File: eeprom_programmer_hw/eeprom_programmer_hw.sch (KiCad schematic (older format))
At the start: 8 parts

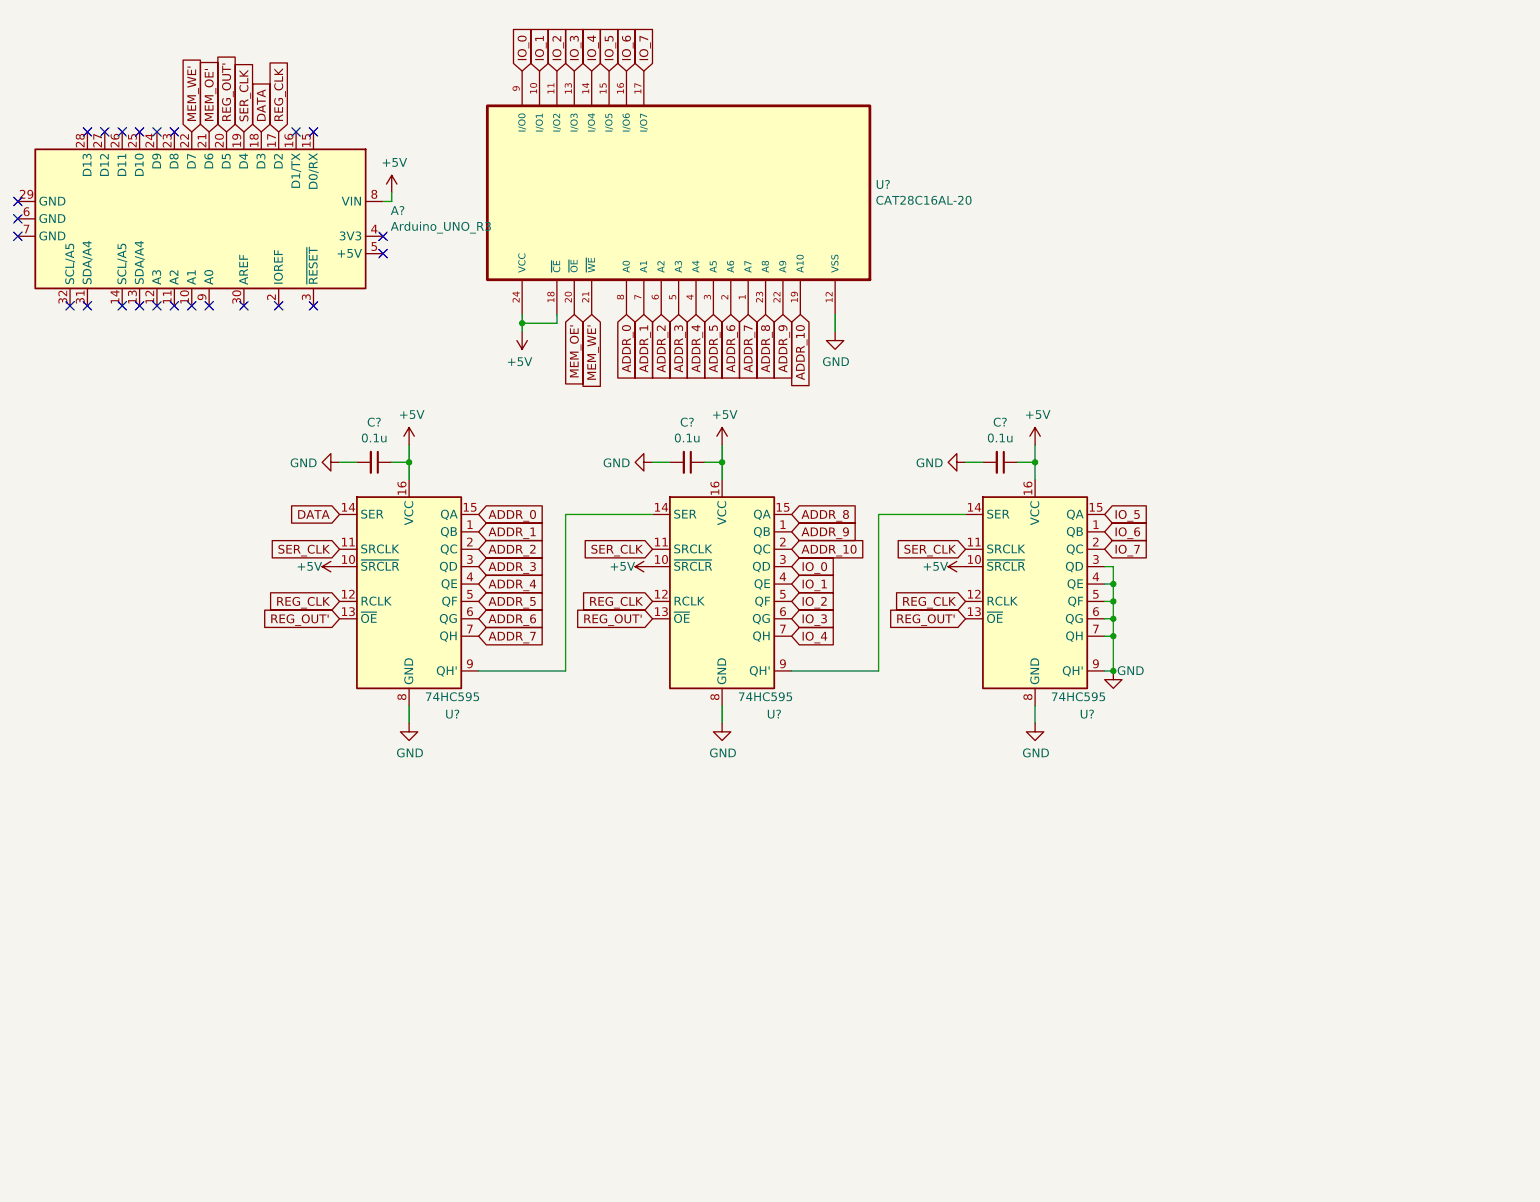
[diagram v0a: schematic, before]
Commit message: Added tri-state buffers to regulate output of shift registers when interating with eeprom I/O.
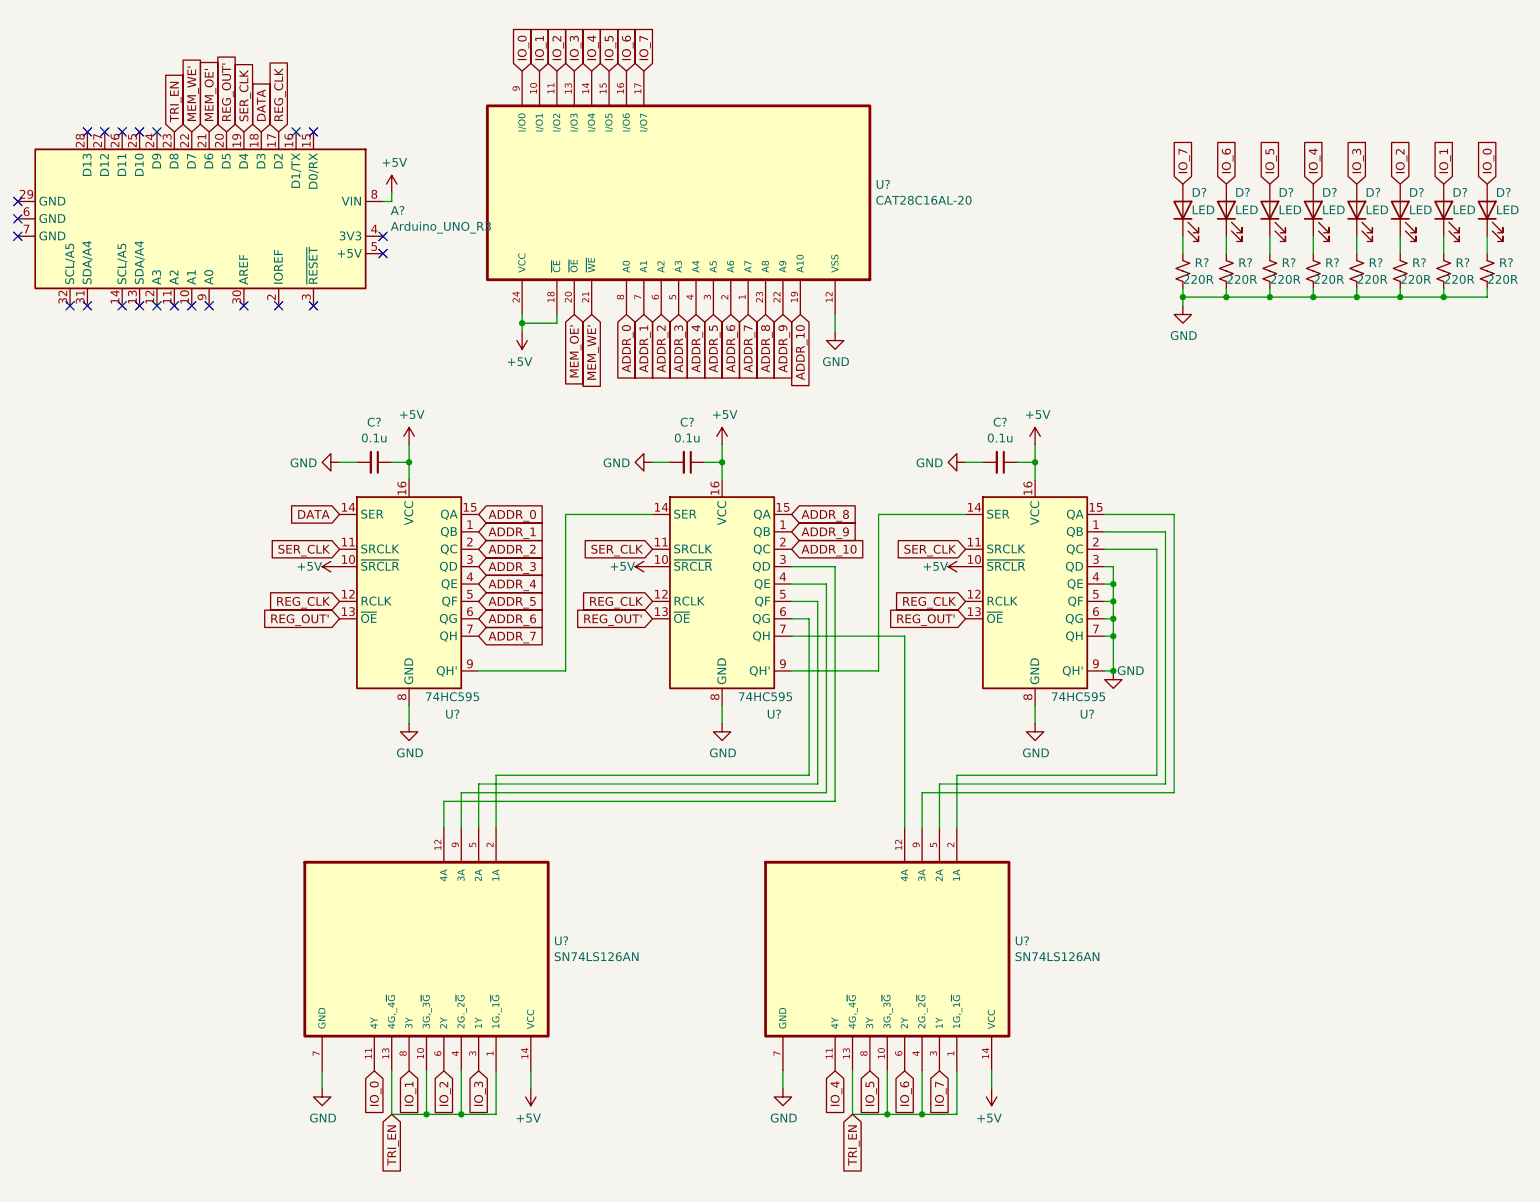
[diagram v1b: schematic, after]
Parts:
- added D? (x8): LED, symbol Device:LED
- added R? (x8): 220R, symbol Device:R_Small_US
- added U? (x2): SN74LS126AN, DIP794W45P254L1969H508Q14, symbol SN74LS126AN:SN74LS126AN
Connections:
- net +5V: now also U?.14 (VCC), U?.14 (VCC)
- net GND: now also R?.2, R?.2, R?.2, R?.2, R?.2, R?.2, R?.2, R?.2, U?.7 (GND), U?.7 (GND)
- net IO_0: now also D?.2 (A), U?.11 (4Y); no longer U?.3 (QD)
- net IO_1: now also D?.2 (A), U?.8 (3Y); no longer U?.4 (QE)
- net IO_2: now also D?.2 (A), U?.6 (2Y); no longer U?.5 (QF)
- net IO_3: now also D?.2 (A), U?.3 (1Y); no longer U?.6 (QG)
- net IO_4: now also D?.2 (A), U?.11 (4Y); no longer U?.7 (QH)
- net IO_5: now also D?.2 (A), U?.8 (3Y); no longer U?.15 (QA)
- net IO_6: now also D?.2 (A), U?.6 (2Y); no longer U?.1 (QB)
- net IO_7: now also D?.2 (A), U?.3 (1Y); no longer U?.2 (QC)
- net TRI_EN: now reaches A?.23 (D8)
- net TRI_EN: now also U?.1 (1G,_1~G), U?.1 (1G,_1~G), U?.10 (3G,_3~G), U?.10 (3G,_3~G), U?.13 (4G,_4~G), U?.13 (4G,_4~G), U?.4 (2G._2~G), U?.4 (2G._2~G)
- new net: U?.12 (4A), U?.3 (QD)
- new net: U?.4 (QE), U?.9 (3A)
- new net: U?.5 (2A), U?.5 (QF)
- new net: U?.2 (1A), U?.6 (QG)
- new net: U?.12 (4A), U?.7 (QH)
- new net: U?.1 (QB), U?.5 (2A)
- new net: U?.15 (QA), U?.9 (3A)
- new net: U?.2 (1A), U?.2 (QC)
- new net: D?.1 (K), R?.1 (x8)
- no-connect marks 24 -> 23
